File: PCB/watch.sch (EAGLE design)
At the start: 12 parts, among them IC1 ISL1209, Q1 IRFD9210, U2 MKL27Z256VLH4

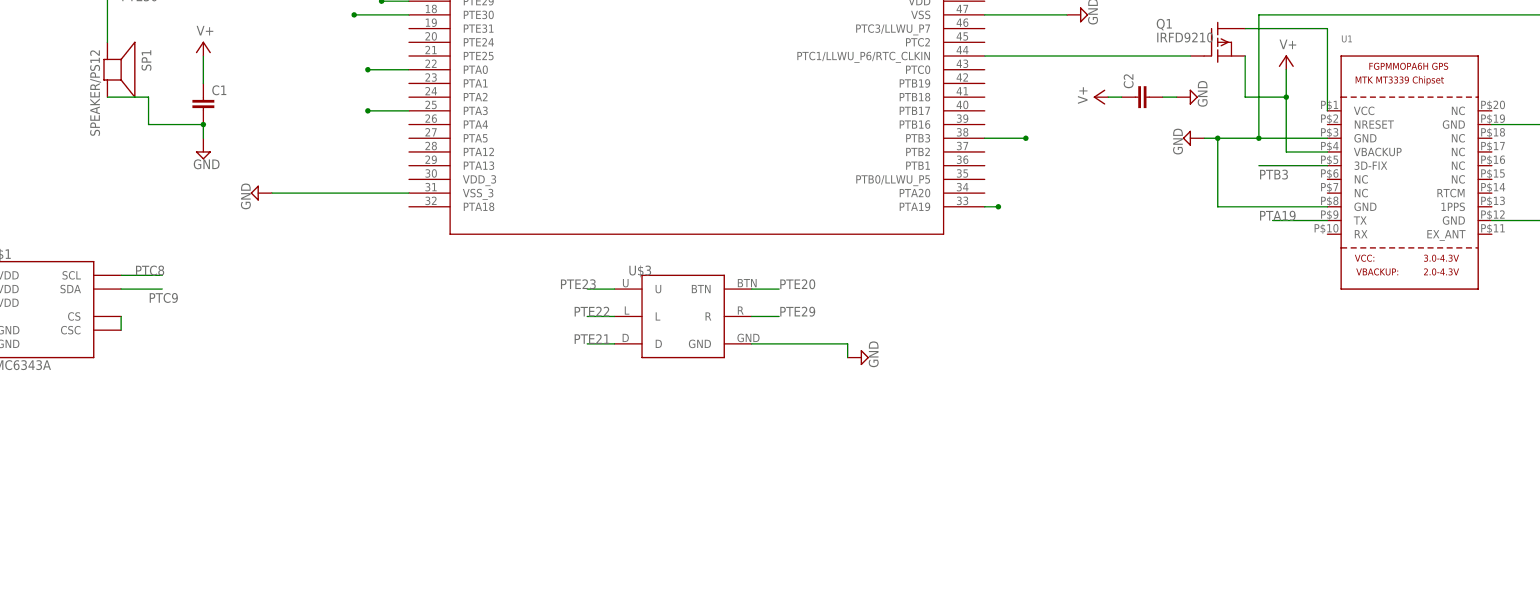
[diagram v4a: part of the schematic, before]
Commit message: added charging unit
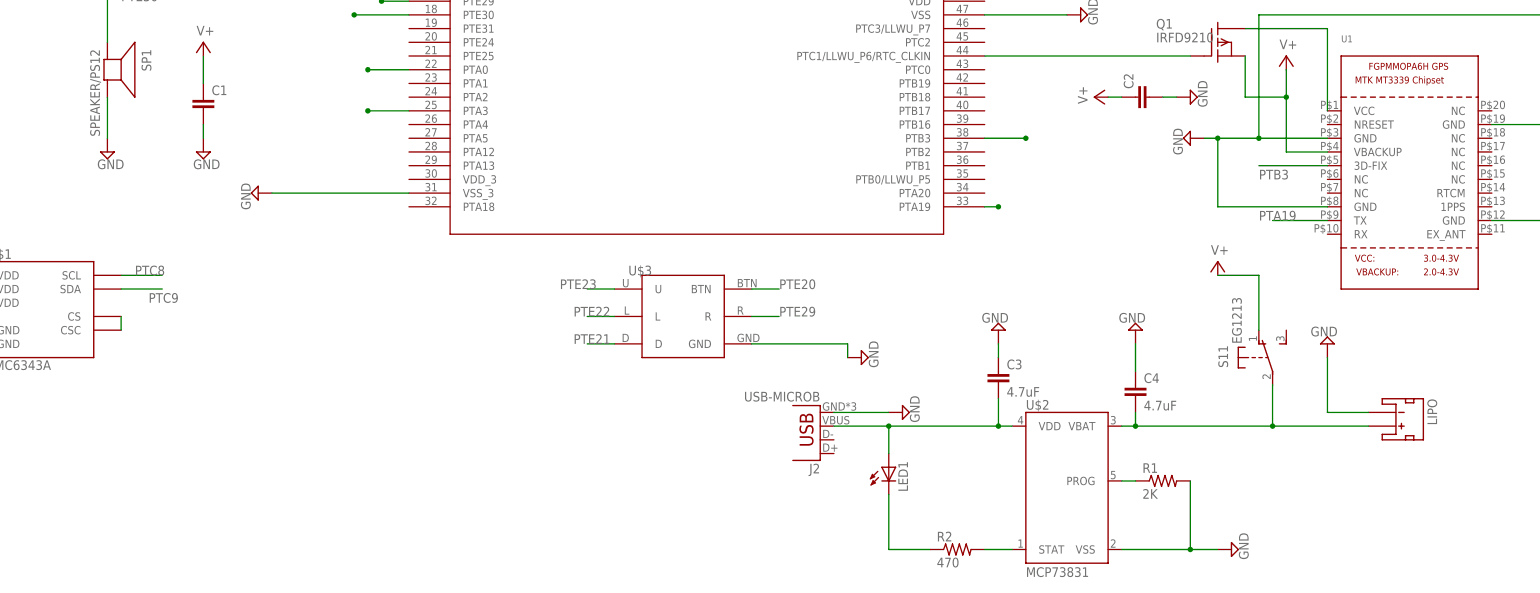
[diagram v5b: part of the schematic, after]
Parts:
- added C3, C4: 4.7uF, SparkFun-Capacitors:0.1UF-25V(+80/-20%)(0603)
- added J2: USB-MICROB, SparkFun-Connectors:USB-MICROB
- added LED1: (no value), eagle-ltspice:LED_ESML0603
- added LIPO: (no value), SparkFun-Connectors:JST_2MM_MALE
- added R1: 2K, SparkFun-Resistors:RESISTOR0603
- added R2: 470, SparkFun-Resistors:RESISTOR0603
- added S1: EG1213, adafruit:EG1213
- added U$2: MCP73831, GeekAmmo:MCP73831
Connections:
- new net N$3: C4.2, LIPO.+, S11.P, U$2.VBAT
- new net N$4: C3.2, J2.VBUS, LED1.A, U$2.VDD
- new net N$5: LED1.C, R2.1
- new net N$7: R2.2, U$2.STAT
- new net N$8: R1.1, U$2.PROG
- net GND: now also C3.1, C4.1, J2.GND, LIPO.-, R1.2, U$2.VSS
- net V+: now also S11.O

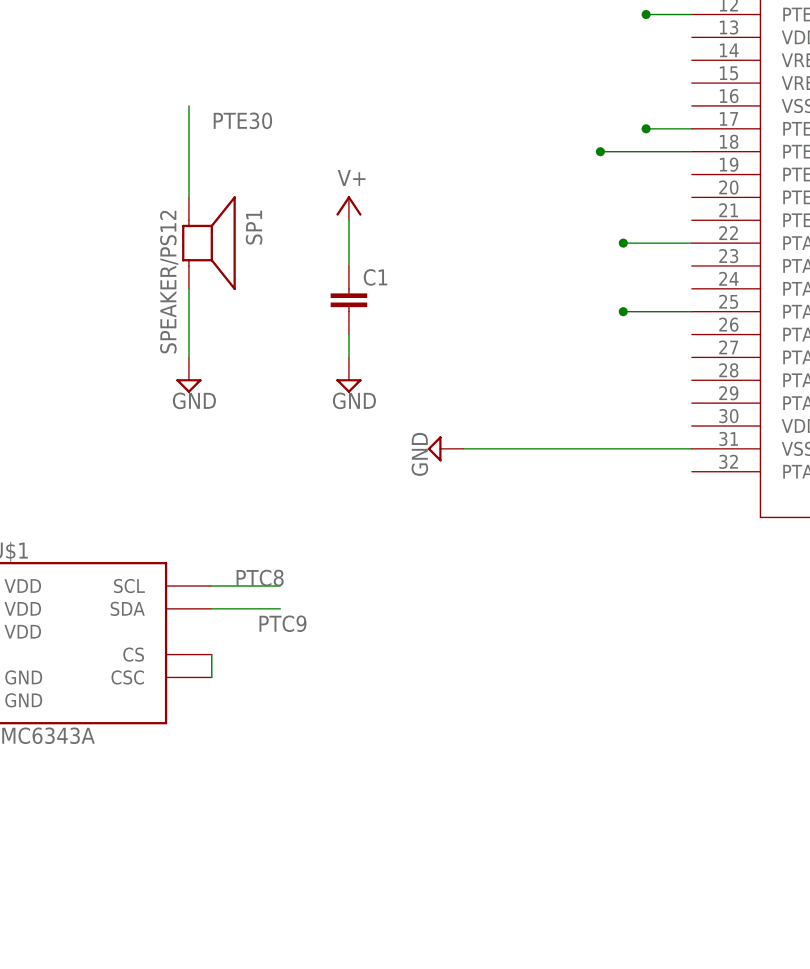
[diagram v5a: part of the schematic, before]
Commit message: added labels
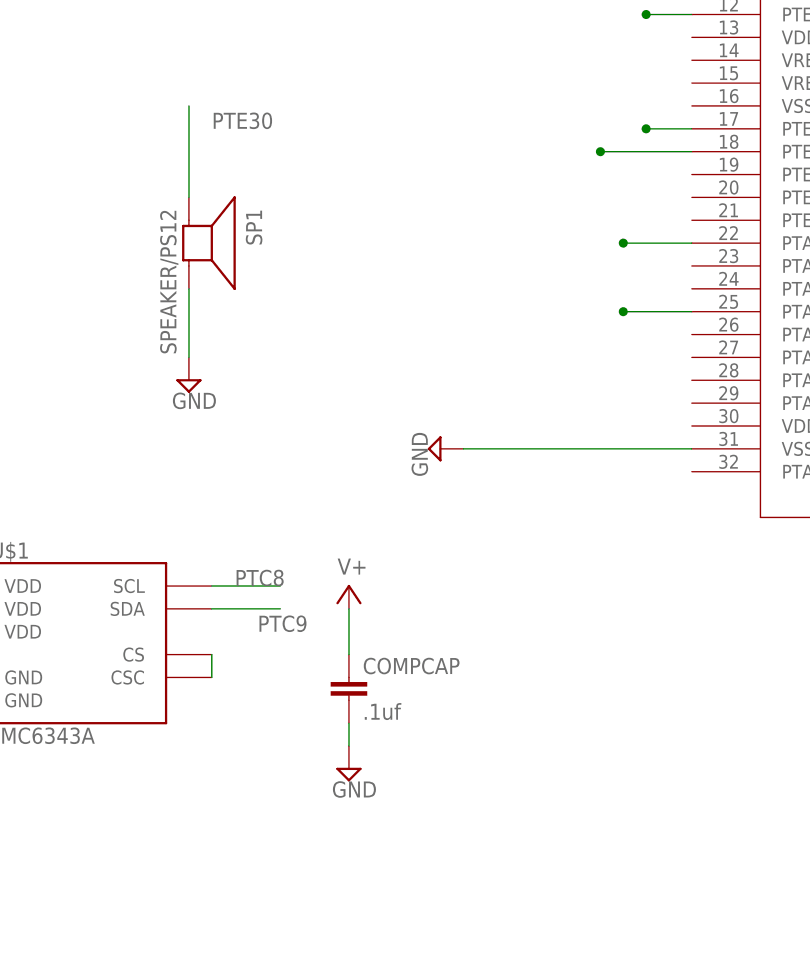
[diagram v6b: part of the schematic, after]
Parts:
- removed C1: (no value), SparkFun:CAP0603
- added COMPCAP: .1uf, SparkFun:CAP0603
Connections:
- net GND: now also COMPCAP.2; no longer C1.2
- net V+: now also COMPCAP.1; no longer C1.1
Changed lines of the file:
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@@
 <part name="DISP2" library="SparkFun-Displays" deviceset="7-SEGMENT-4DIGIT-COUNTER" device="-HP-BUBBLE"/>
 <part name="U$1" library="SparkFun" deviceset="HMC6343" device="A"/>
-<part name="C1" library="SparkFun" deviceset="CAP" device="0603"/>
+<part name="COMPCAP" library="SparkFun" deviceset="CAP" device="0603" value=".1uf"/>
 <part name="SUPPLY1" library="supply2" deviceset="GND" device=""/>
 <part name="SUPPLY2" library="supply2" deviceset="GND" device=""/>
@@
 <instance part="DISP2" gate="G$1" x="60.96" y="195.58"/>
 <instance part="U$1" gate="G$1" x="-93.98" y="66.04"/>
-<instance part="C1" gate="G$1" x="-63.5" y="101.6"/>
+<instance part="COMPCAP" gate="G$1" x="-63.5" y="58.42"/>
 <instance part="SUPPLY1" gate="GND" x="-124.46" y="58.42"/>
-<instance part="SUPPLY2" gate="GND" x="-63.5" y="93.98"/>
-<instance part="SUPPLY3" gate="1" x="-63.5" y="114.3"/>
+<instance part="SUPPLY2" gate="GND" x="-63.5" y="50.8"/>
+<instance part="SUPPLY3" gate="1" x="-63.5" y="71.12"/>
 <instance part="SUPPLY4" gate="GND" x="58.42" y="55.88" rot="R90"/>
 <instance part="U1" gate="G$1" x="160.02" y="91.44"/>
@@
 <segment>
 <pinref part="SUPPLY2" gate="GND" pin="GND"/>
-<pinref part="C1" gate="G$1" pin="2"/>
-<wire x1="-63.5" y1="99.06" x2="-63.5" y2="96.52" width="0.1524" layer="91"/>
+<pinref part="COMPCAP" gate="G$1" pin="2"/>
+<wire x1="-63.5" y1="55.88" x2="-63.5" y2="53.34" width="0.1524" layer="91"/>
 </segment>
 <segment>
@@
 <net name="V+" class="0">
 <segment>
-<pinref part="C1" gate="G$1" pin="1"/>
+<pinref part="COMPCAP" gate="G$1" pin="1"/>
 <pinref part="SUPPLY3" gate="1" pin="V+"/>
-<wire x1="-63.5" y1="106.68" x2="-63.5" y2="111.76" width="0.1524" layer="91"/>
-</segment>
-<segment>
+<wire x1="-63.5" y1="63.5" x2="-63.5" y2="68.58" width="0.1524" layer="91"/>
+</segment>
+<segment>

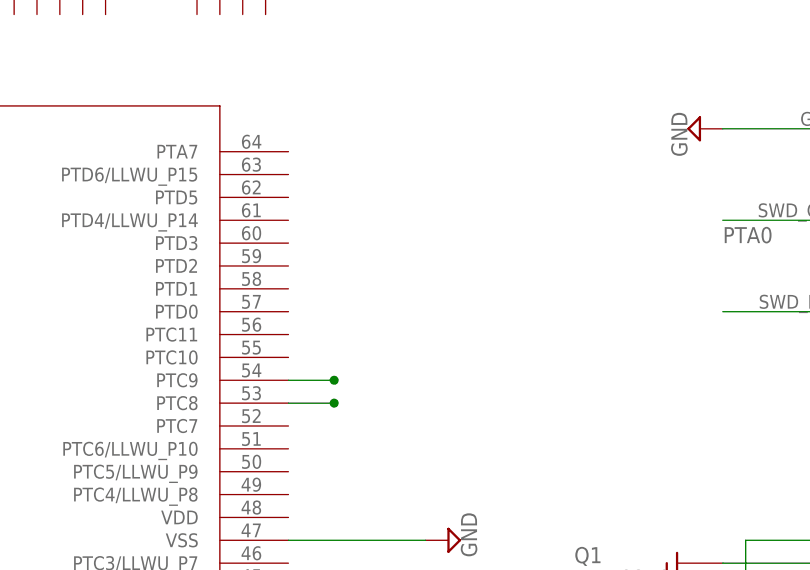
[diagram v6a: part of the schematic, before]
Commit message: added pull up resistors
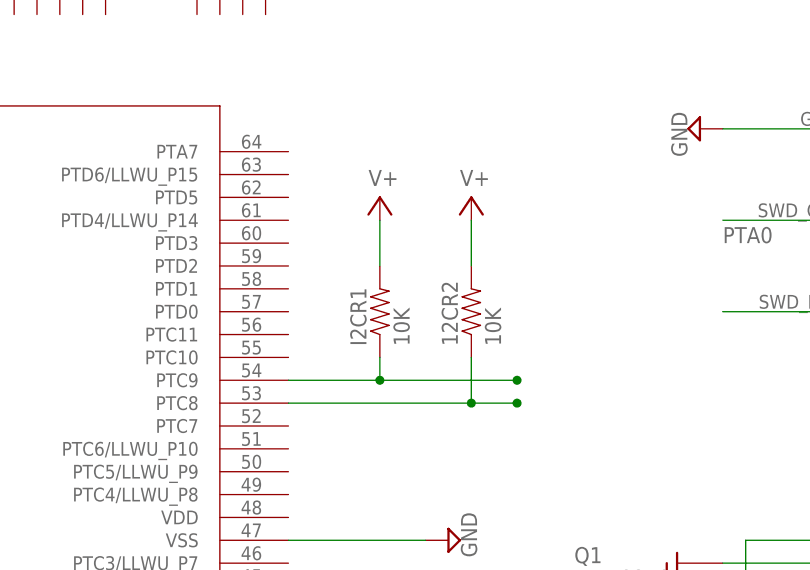
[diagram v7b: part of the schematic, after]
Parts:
- added 12CR2, I2CR1: 10K, SparkFun-Resistors:RESISTOR0603
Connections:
- net PTC8: now also 12CR2.1
- net PTC9: now also I2CR1.1
- net V+: now also 12CR2.2, I2CR1.2
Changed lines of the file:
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@@
 <part name="SUPPLY20" library="supply2" deviceset="V+" device=""/>
 <part name="SUPPLY21" library="supply2" deviceset="GND" device=""/>
+<part name="I2CR1" library="SparkFun-Resistors" deviceset="RESISTOR" device="0603" value="10K"/>
+<part name="12CR2" library="SparkFun-Resistors" deviceset="RESISTOR" device="0603" value="10K"/>
+<part name="SUPPLY22" library="supply2" deviceset="V+" device=""/>
+<part name="SUPPLY23" library="supply2" deviceset="V+" device=""/>
 </parts>
 <sheets>
@@
 <instance part="SUPPLY20" gate="1" x="124.46" y="73.66"/>
 <instance part="SUPPLY21" gate="GND" x="-81.28" y="93.98"/>
+<instance part="I2CR1" gate="G$1" x="91.44" y="144.78" rot="R90"/>
+<instance part="12CR2" gate="G$1" x="101.6" y="144.78" rot="R90"/>
+<instance part="SUPPLY22" gate="1" x="91.44" y="157.48"/>
+<instance part="SUPPLY23" gate="1" x="101.6" y="157.48"/>
 </instances>
 <busses>
@@
 <wire x1="132.08" y1="71.12" x2="132.08" y2="60.96" width="0.1524" layer="91"/>
 </segment>
+<segment>
+<pinref part="SUPPLY22" gate="1" pin="V+"/>
+<pinref part="I2CR1" gate="G$1" pin="2"/>
+<wire x1="91.44" y1="154.94" x2="91.44" y2="149.86" width="0.1524" layer="91"/>
+</segment>
+<segment>
+<pinref part="SUPPLY23" gate="1" pin="V+"/>
+<pinref part="12CR2" gate="G$1" pin="2"/>
+<wire x1="101.6" y1="154.94" x2="101.6" y2="149.86" width="0.1524" layer="91"/>
+</segment>
 </net>
 <net name="PTA19" class="0">
@@
 <segment>
 <pinref part="U2" gate="A" pin="PTC8"/>
-<wire x1="81.28" y1="134.62" x2="86.36" y2="134.62" width="0.1524" layer="91"/>
-<junction x="86.36" y="134.62"/>
+<wire x1="81.28" y1="134.62" x2="101.6" y2="134.62" width="0.1524" layer="91"/>
+<junction x="106.68" y="134.62"/>
+<pinref part="12CR2" gate="G$1" pin="1"/>
+<wire x1="101.6" y1="134.62" x2="106.68" y2="134.62" width="0.1524" layer="91"/>
+<wire x1="101.6" y1="139.7" x2="101.6" y2="134.62" width="0.1524" layer="91"/>
+<junction x="101.6" y="134.62"/>
 </segment>
 <segment>
@@
 <segment>
 <pinref part="U2" gate="A" pin="PTC9"/>
-<wire x1="81.28" y1="137.16" x2="86.36" y2="137.16" width="0.1524" layer="91"/>
-<junction x="86.36" y="137.16"/>
-</segment>
-<segment>
+<wire x1="81.28" y1="137.16" x2="91.44" y2="137.16" width="0.1524" layer="91"/>
+<junction x="106.68" y="137.16"/>
+<pinref part="I2CR1" gate="G$1" pin="1"/>
+<wire x1="91.44" y1="137.16" x2="106.68" y2="137.16" width="0.1524" layer="91"/>
+<wire x1="91.44" y1="139.7" x2="91.44" y2="137.16" width="0.1524" layer="91"/>
+<junction x="91.44" y="137.16"/>
+</segment>
+<segment>

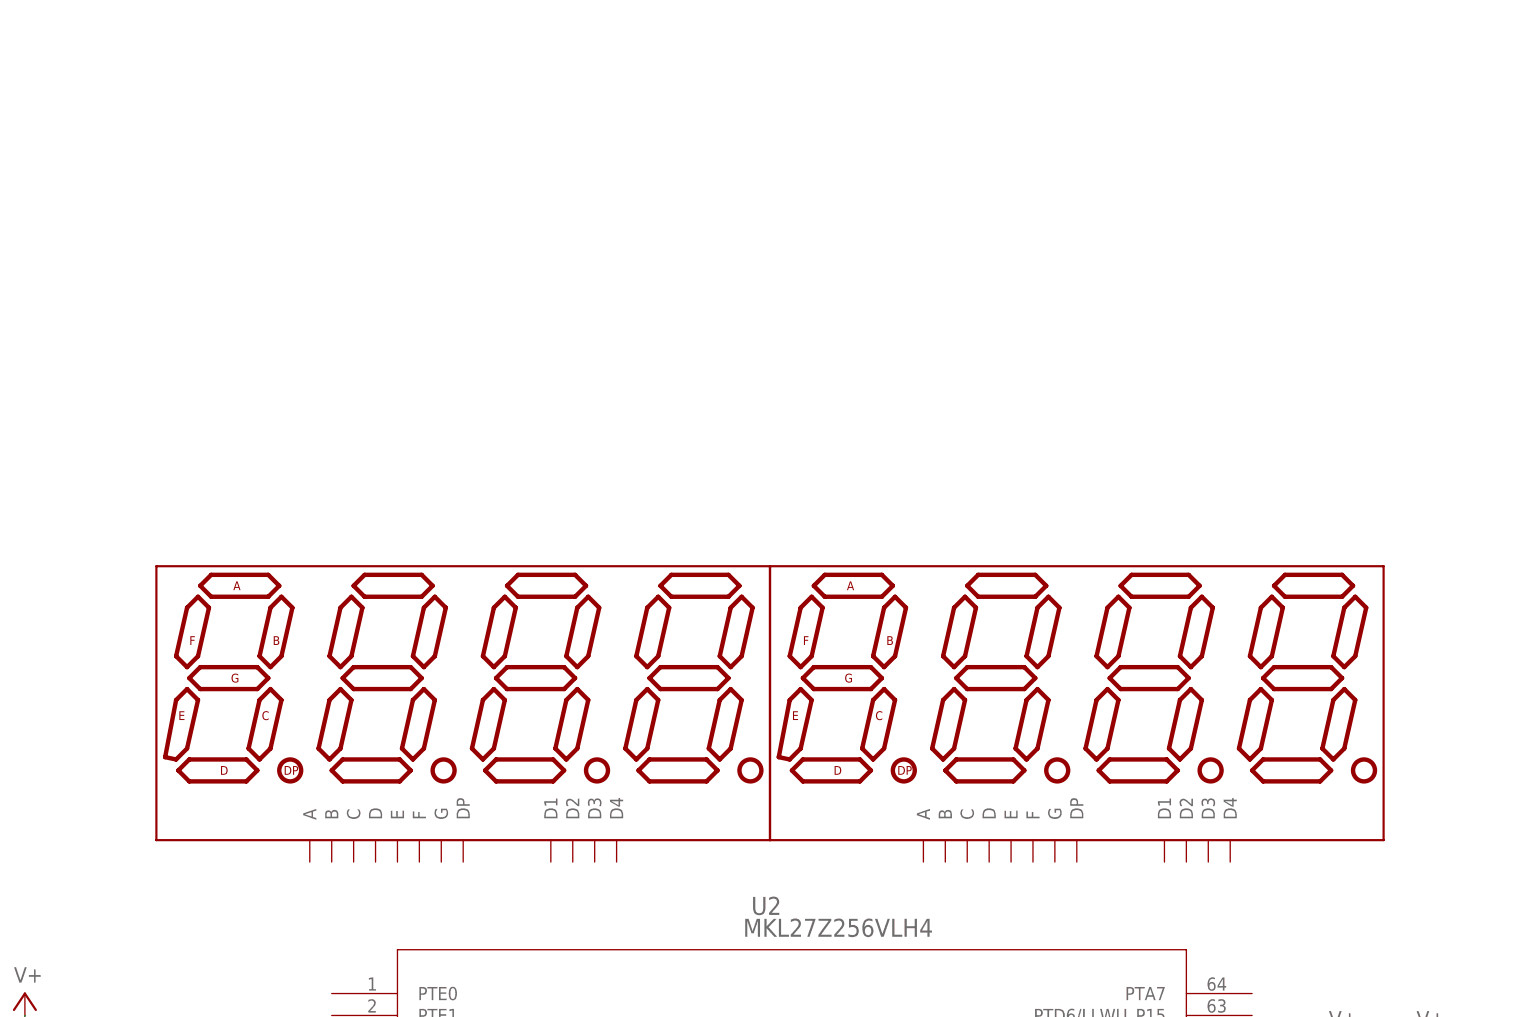
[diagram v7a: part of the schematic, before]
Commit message: added shift regs to board
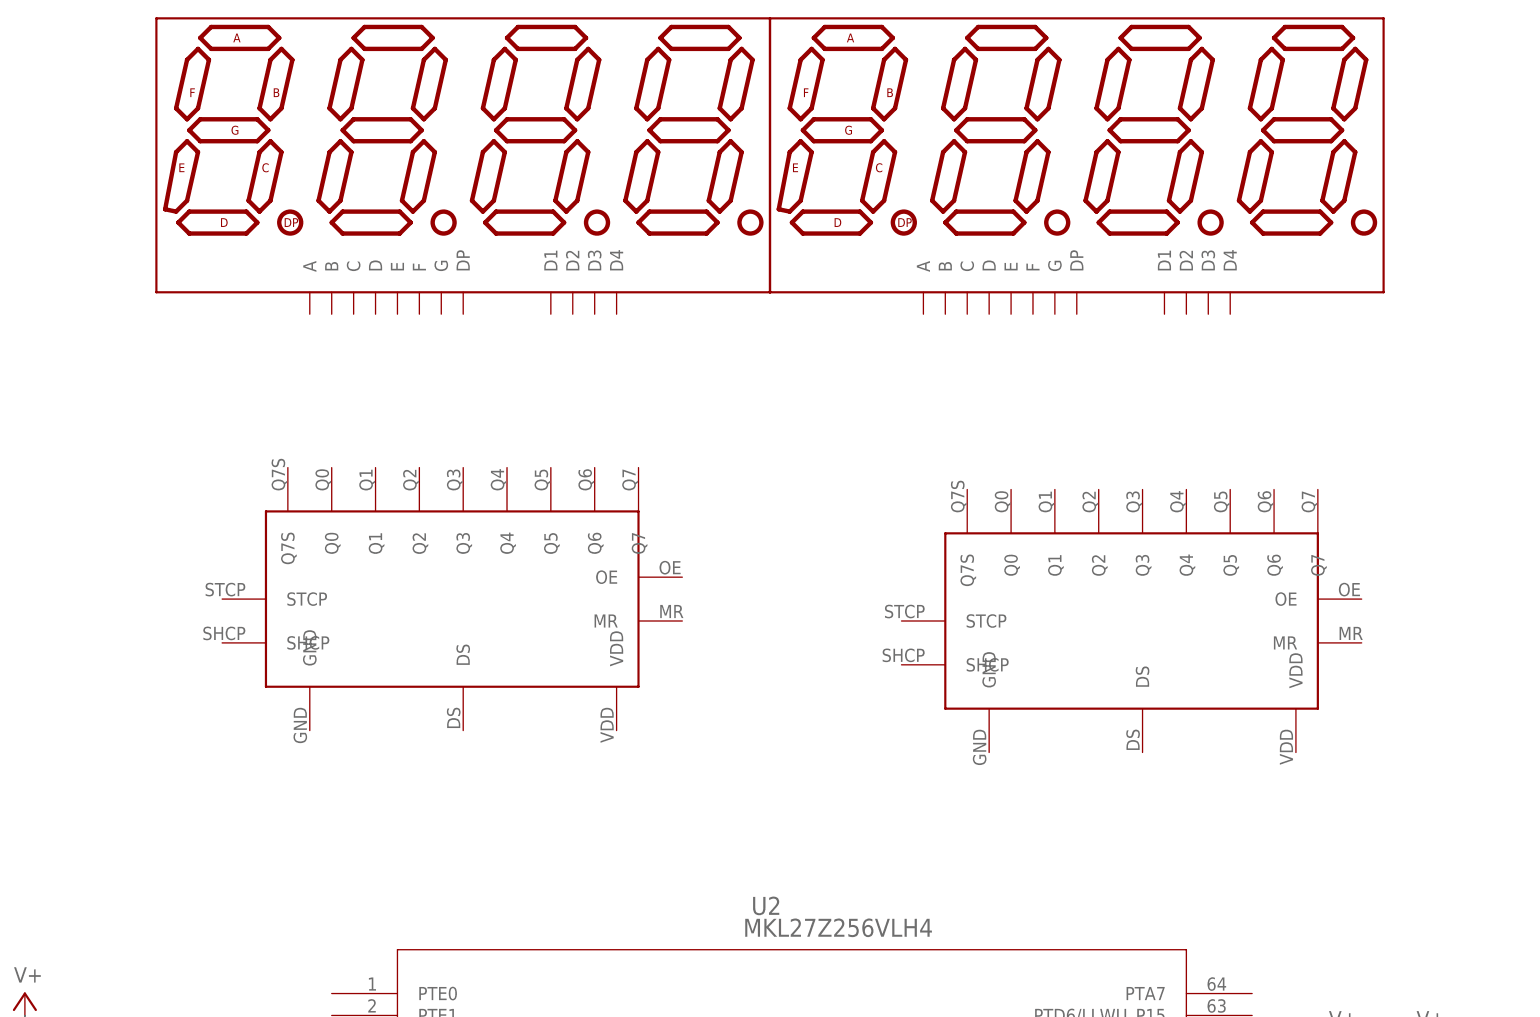
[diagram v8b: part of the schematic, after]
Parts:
- added U$4, U$5: 74HC595PW, BOS_libs:74HC595PW
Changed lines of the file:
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@@
 <part name="SUPPLY22" library="supply2" deviceset="V+" device=""/>
 <part name="SUPPLY23" library="supply2" deviceset="V+" device=""/>
+<part name="U$4" library="BOS_libs" deviceset="74HC595PW" device=""/>
+<part name="U$5" library="BOS_libs" deviceset="74HC595PW" device=""/>
 </parts>
 <sheets>
@@
 </plain>
 <instances>
-<instance part="DISP1" gate="G$1" x="-10.16" y="195.58"/>
-<instance part="DISP2" gate="G$1" x="60.96" y="195.58"/>
+<instance part="DISP1" gate="G$1" x="-10.16" y="259.08"/>
+<instance part="DISP2" gate="G$1" x="60.96" y="259.08"/>
 <instance part="U$1" gate="G$1" x="-93.98" y="66.04"/>
 <instance part="COMPCAP" gate="G$1" x="-63.5" y="58.42"/>
@@
 <instance part="SUPPLY22" gate="1" x="91.44" y="157.48"/>
 <instance part="SUPPLY23" gate="1" x="101.6" y="157.48"/>
+<instance part="U$4" gate="G$1" x="-15.24" y="208.28" rot="R90"/>
+<instance part="U$5" gate="G$1" x="63.5" y="205.74" rot="R90"/>
 </instances>
 <busses>
